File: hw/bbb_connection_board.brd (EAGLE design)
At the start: 20 x 64 mm, 11 parts, among them P8 MA23-2

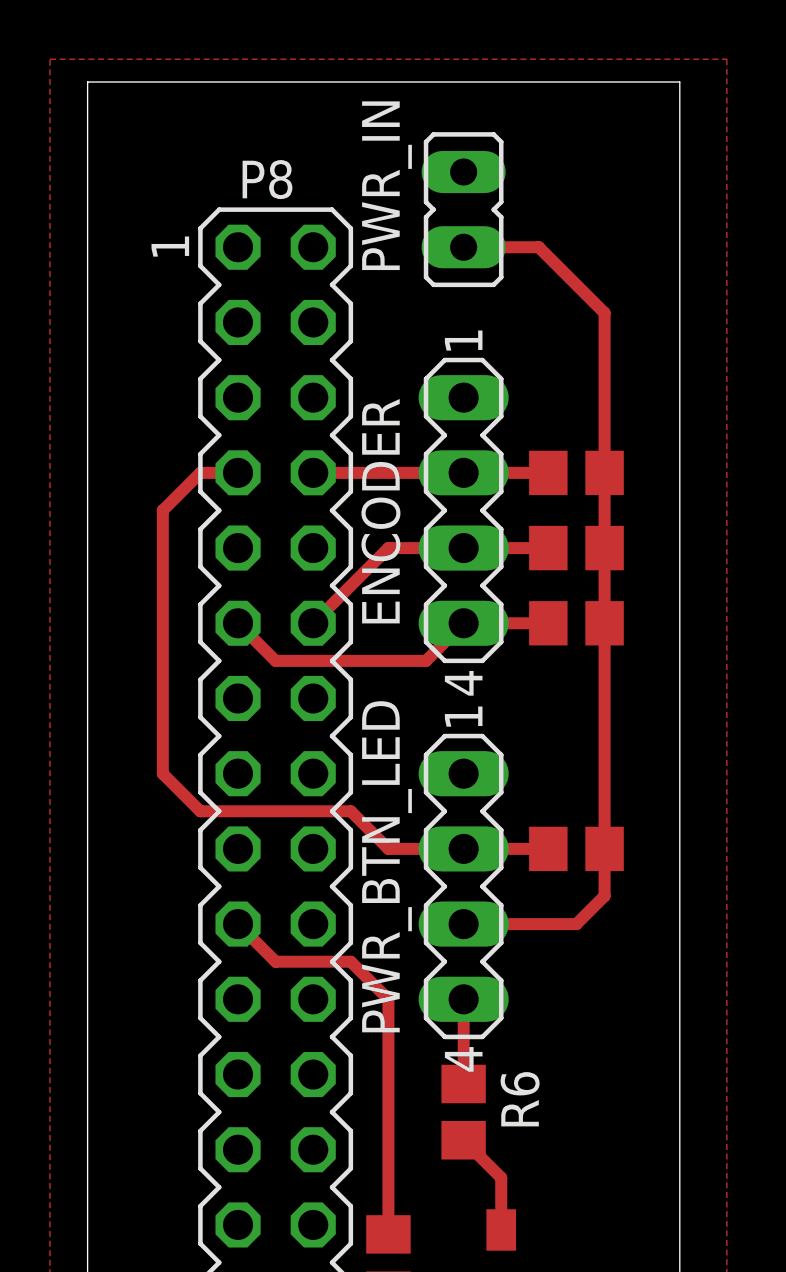
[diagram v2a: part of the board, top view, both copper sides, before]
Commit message: move connectors to bottom layer
the connector to the bbb also needs to be mounted on the bottom side, but can't be simply mirrored, since that would change the pinout
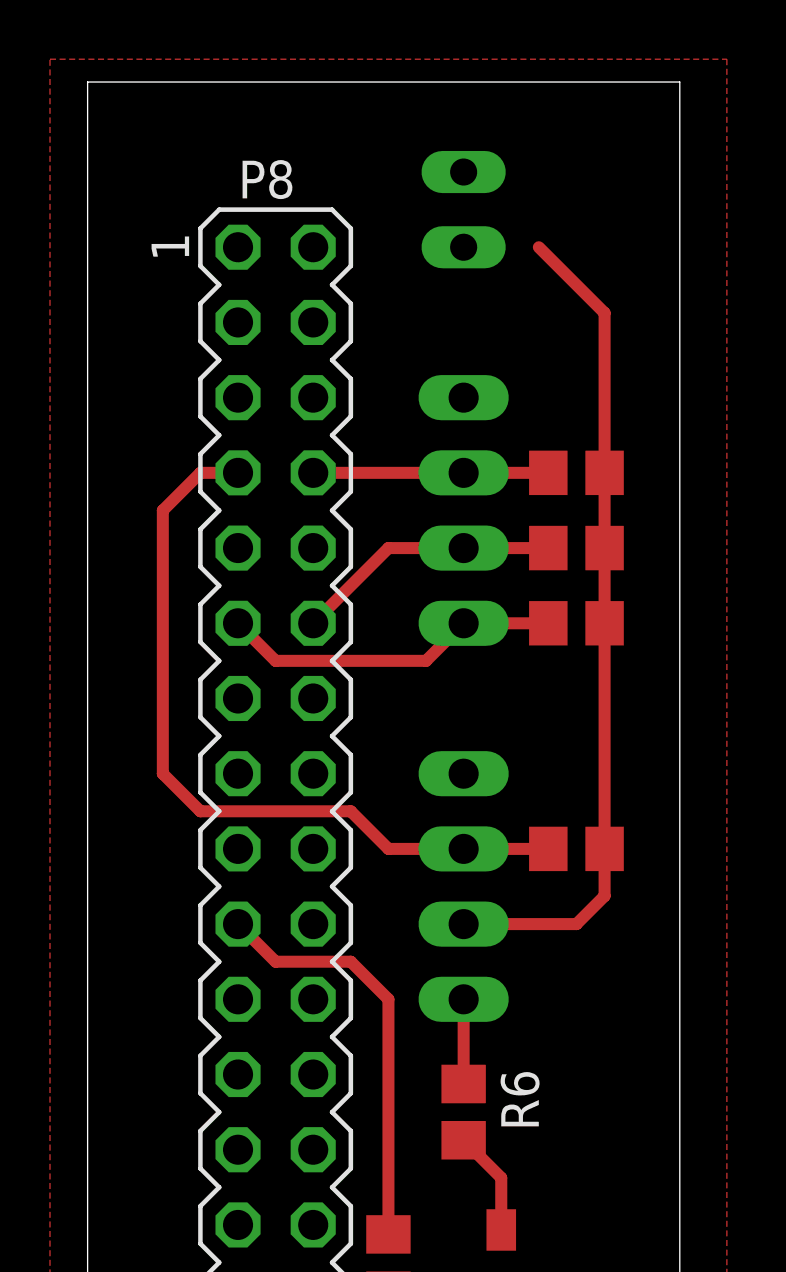
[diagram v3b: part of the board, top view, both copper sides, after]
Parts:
- flipped ENCODER to the bottom
- flipped PWR_BTN_LED to the bottom
- flipped PWR_IN to the bottom
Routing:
- net +3V3: track 30.5 -> 28.0 mm
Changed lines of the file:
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@@
 <attribute name="VALUE" x="2.159" y="5.08" size="1.27" layer="27" ratio="10" rot="R270"/>
 </element>
-<element name="PWR_IN" library="jumper" package="JP1" value="" x="12.7" y="59.69" smashed="yes" rot="R180">
-<attribute name="NAME" x="9.271" y="63.5" size="1.27" layer="25" ratio="10" rot="R270"/>
-<attribute name="VALUE" x="9.779" y="62.23" size="1.27" layer="27" ratio="10" rot="R270"/>
+<element name="PWR_IN" library="jumper" package="JP1" value="" x="12.7" y="59.69" smashed="yes" rot="MR180">
+<attribute name="NAME" x="14.351" y="55.88" size="1.27" layer="26" ratio="10" rot="MR90"/>
+<attribute name="VALUE" x="15.621" y="62.23" size="1.27" layer="28" ratio="10" rot="MR270"/>
 </element>
 <element name="R1" library="rcl" package="R0805" value="10k" x="16.51" y="38.1" smashed="yes">
@@
 <attribute name="VALUE" x="15.875" y="43.18" size="1.27" layer="27"/>
 </element>
-<element name="ENCODER" library="con-lstb" package="MA04-1" value="" x="12.7" y="49.53" smashed="yes" rot="R270">
-<attribute name="OC_NEWARK" value="unknown" x="12.7" y="49.53" size="1.778" layer="27" rot="R270" display="off"/>
-<attribute name="MPN" value="" x="12.7" y="49.53" size="1.778" layer="27" rot="R270" display="off"/>
-<attribute name="MF" value="" x="12.7" y="49.53" size="1.778" layer="27" rot="R270" display="off"/>
-<attribute name="OC_FARNELL" value="unknown" x="12.7" y="49.53" size="1.778" layer="27" rot="R270" display="off"/>
-<attribute name="NAME" x="9.271" y="53.34" size="1.27" layer="25" ratio="10" rot="R270"/>
-<attribute name="VALUE" x="14.351" y="48.895" size="1.27" layer="27" ratio="10" rot="R270"/>
+<element name="ENCODER" library="con-lstb" package="MA04-1" value="" x="12.7" y="49.53" smashed="yes" rot="MR270">
+<attribute name="OC_NEWARK" value="unknown" x="12.7" y="49.53" size="1.778" layer="28" rot="MR270" display="off"/>
+<attribute name="MPN" value="" x="12.7" y="49.53" size="1.778" layer="28" rot="MR270" display="off"/>
+<attribute name="MF" value="" x="12.7" y="49.53" size="1.778" layer="28" rot="MR270" display="off"/>
+<attribute name="OC_FARNELL" value="unknown" x="12.7" y="49.53" size="1.778" layer="28" rot="MR270" display="off"/>
+<attribute name="NAME" x="16.129" y="54.61" size="1.27" layer="26" ratio="10" rot="MR270"/>
+<attribute name="VALUE" x="11.049" y="48.895" size="1.27" layer="28" ratio="10" rot="MR270"/>
 </element>
-<element name="PWR_BTN_LED" library="con-lstb" package="MA04-1" value="" x="12.7" y="36.83" smashed="yes" rot="R270">
-<attribute name="OC_NEWARK" value="unknown" x="12.7" y="36.83" size="1.778" layer="27" rot="R270" display="off"/>
-<attribute name="MPN" value="" x="12.7" y="36.83" size="1.778" layer="27" rot="R270" display="off"/>
-<attribute name="MF" value="" x="12.7" y="36.83" size="1.778" layer="27" rot="R270" display="off"/>
-<attribute name="OC_FARNELL" value="unknown" x="12.7" y="36.83" size="1.778" layer="27" rot="R270" display="off"/>
-<attribute name="NAME" x="9.271" y="43.18" size="1.27" layer="25" ratio="10" rot="R270"/>
-<attribute name="VALUE" x="14.351" y="36.195" size="1.27" layer="27" ratio="10" rot="R270"/>
+<element name="PWR_BTN_LED" library="con-lstb" package="MA04-1" value="" x="12.7" y="36.83" smashed="yes" rot="MR270">
+<attribute name="OC_NEWARK" value="unknown" x="12.7" y="36.83" size="1.778" layer="28" rot="MR270" display="off"/>
+<attribute name="MPN" value="" x="12.7" y="36.83" size="1.778" layer="28" rot="MR270" display="off"/>
+<attribute name="MF" value="" x="12.7" y="36.83" size="1.778" layer="28" rot="MR270" display="off"/>
+<attribute name="OC_FARNELL" value="unknown" x="12.7" y="36.83" size="1.778" layer="28" rot="MR270" display="off"/>
+<attribute name="NAME" x="16.129" y="43.18" size="1.27" layer="26" ratio="10" rot="MR270"/>
+<attribute name="VALUE" x="11.049" y="36.195" size="1.27" layer="28" ratio="10" rot="MR270"/>
 </element>
 <element name="T1" library="transistor" package="SOT23-BEC" value="" x="13.97" y="24.13" smashed="yes">
@@
 <contactref element="R4" pad="2"/>
 <contactref element="PWR_BTN_LED" pad="3"/>
-<wire x1="12.7" y1="58.42" x2="15.24" y2="58.42" width="0.4064" layer="1"/>
 <wire x1="15.24" y1="58.42" x2="17.46" y2="56.2" width="0.4064" layer="1"/>
 <wire x1="17.46" y1="50.8" x2="17.46" y2="56.2" width="0.4064" layer="1"/>
@@
 <wire x1="17.46" y1="36.51" x2="16.51" y2="35.56" width="0.4064" layer="1"/>
 <wire x1="16.51" y1="35.56" x2="12.7" y2="35.56" width="0.4064" layer="1"/>
+<wire x1="15.24" y1="58.42" x2="12.7" y2="58.42" width="0" layer="19" extent="1-1"/>
 </signal>
 <signal name="PWR_LED">
@@
 <wire x1="5.08" y1="45.72" x2="6.35" y2="44.45" width="0.4064" layer="1"/>
 <wire x1="6.35" y1="44.45" x2="11.43" y2="44.45" width="0.4064" layer="1"/>
-<wire x1="11.43" y1="44.45" x2="12.7" y2="45.72" width="0.4064" layer="1"/>
 <wire x1="12.7" y1="45.72" x2="15.56" y2="45.72" width="0.4064" layer="1"/>
+<wire x1="12.7" y1="45.72" x2="11.43" y2="44.45" width="0.4064" layer="1"/>
 </signal>
 <signal name="ENCODER_A">
@@
 <contactref element="R3" pad="1"/>
 <contactref element="ENCODER" pad="3"/>
+<wire x1="7.62" y1="45.72" x2="10.16" y2="48.26" width="0.4064" layer="1"/>
+<wire x1="12.7" y1="48.26" x2="10.16" y2="48.26" width="0.4064" layer="1"/>
 <wire x1="12.7" y1="48.26" x2="15.56" y2="48.26" width="0.4064" layer="1"/>
-<wire x1="7.62" y1="45.72" x2="10.16" y2="48.26" width="0.4064" layer="1"/>
-<wire x1="10.16" y1="48.26" x2="12.7" y2="48.26" width="0.4064" layer="1"/>
 </signal>
 <signal name="PWR_BTN">

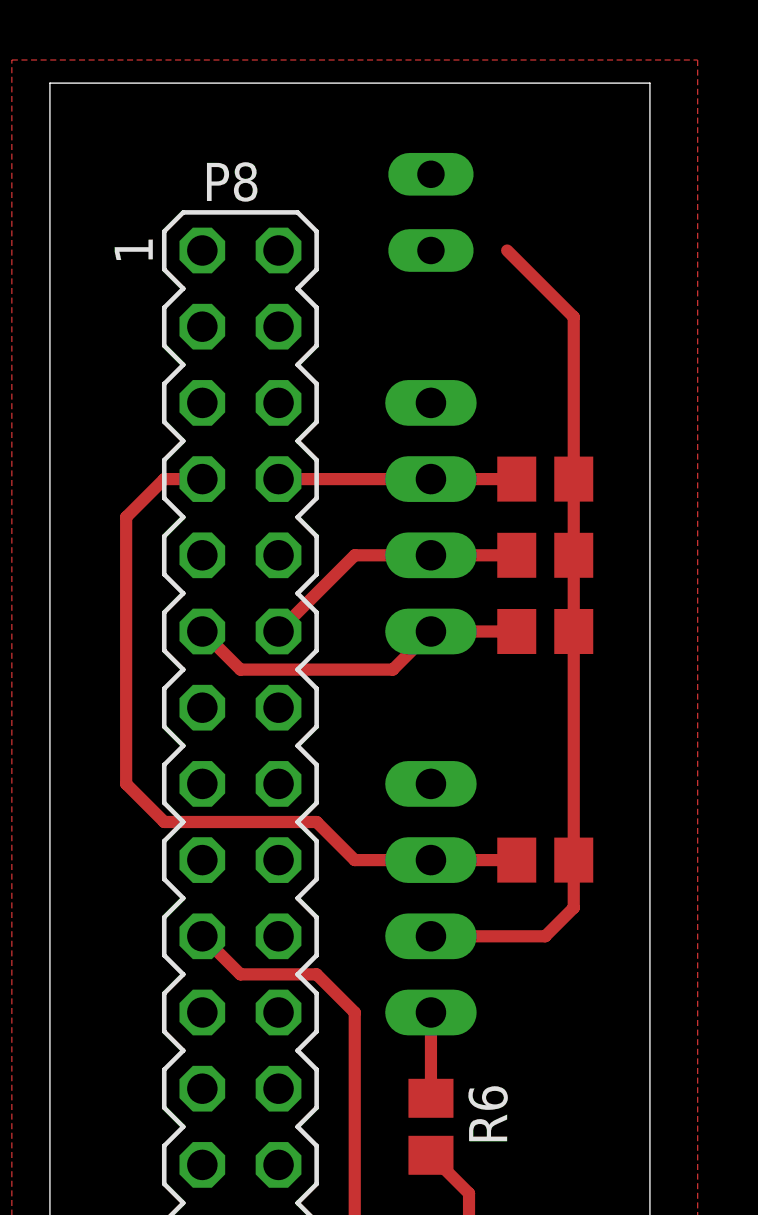
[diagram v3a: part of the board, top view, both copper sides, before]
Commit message: use angled pinheaders
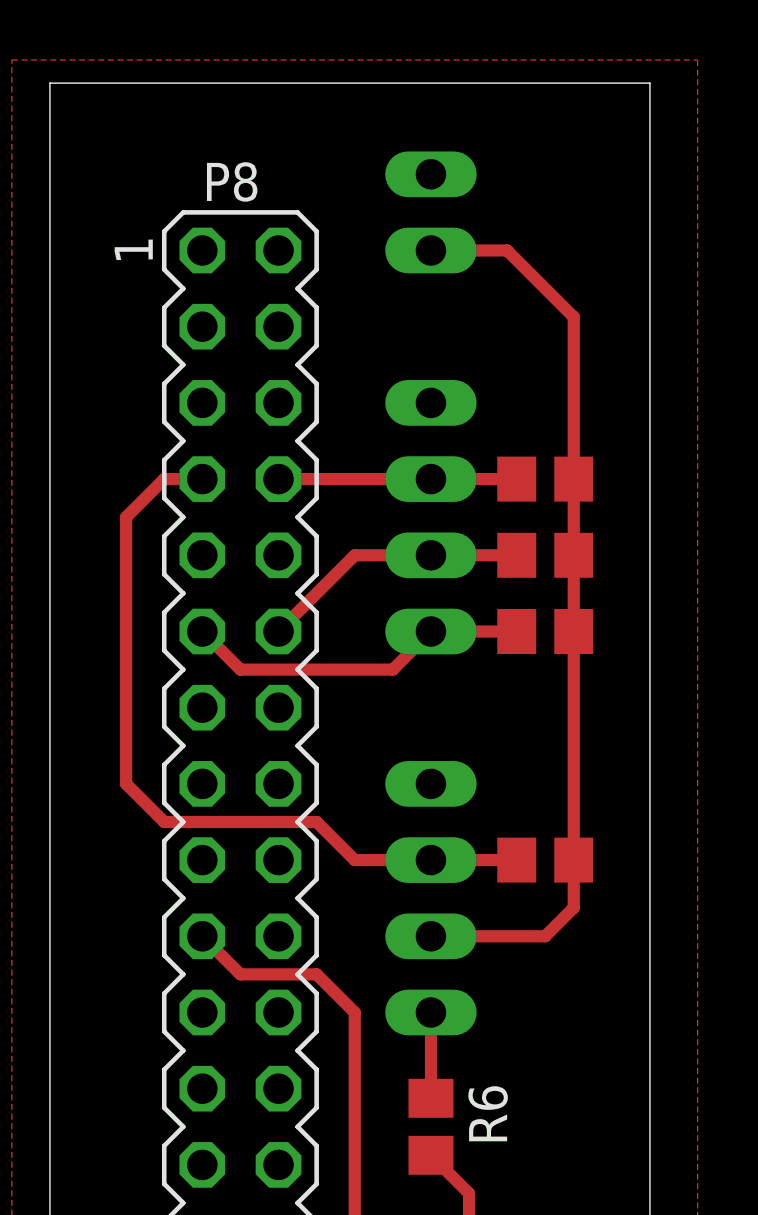
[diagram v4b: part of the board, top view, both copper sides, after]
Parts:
- removed PWR_BTN_LED: (no value), con-lstb:MA04-1
- removed PWR_IN: (no value), jumper:JP1
- added PWN_BTN_LED: (no value), pinhead:1X04/90
- added PWR_CON: (no value), pinhead:1X02/90
- ENCODER: device con-lstb:MA04-1 -> pinhead:1X04/90
- moved ENCODER 3.81 mm to (16.5, 49.5), turned to 90 degrees
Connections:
- net +3V3: now also PWN_BTN_LED.2, PWR_CON.1; no longer PWR_BTN_LED.3, PWR_IN.2
- net ENCODER_A: now also ENCODER.2; no longer ENCODER.3
- net ENCODER_B: now also ENCODER.1; no longer ENCODER.4
- net ENCODER_BTN: now also ENCODER.3; no longer ENCODER.2
- net GND: now also ENCODER.4, PWN_BTN_LED.4, PWR_CON.2; no longer ENCODER.1, PWR_BTN_LED.1, PWR_IN.1
- net LED_OUT: now also PWN_BTN_LED.1; no longer PWR_BTN_LED.4
- net PWR_BTN: now also PWN_BTN_LED.3; no longer PWR_BTN_LED.2
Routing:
- net +3V3: track 28.0 -> 30.5 mm
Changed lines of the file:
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@@
 <attribute name="VALUE" x="2.159" y="5.08" size="1.27" layer="27" ratio="10" rot="R270"/>
-</element>
-<element name="PWR_IN" library="jumper" package="JP1" value="" x="12.7" y="59.69" smashed="yes" rot="MR180">
-<attribute name="NAME" x="14.351" y="55.88" size="1.27" layer="26" ratio="10" rot="MR90"/>
-<attribute name="VALUE" x="15.621" y="62.23" size="1.27" layer="28" ratio="10" rot="MR270"/>
 </element>
 <element name="R1" library="rcl" package="R0805" value="10k" x="16.51" y="38.1" smashed="yes">
@@
 <attribute name="VALUE" x="15.875" y="43.18" size="1.27" layer="27"/>
 </element>
-<element name="ENCODER" library="con-lstb" package="MA04-1" value="" x="12.7" y="49.53" smashed="yes" rot="MR270">
-<attribute name="OC_NEWARK" value="unknown" x="12.7" y="49.53" size="1.778" layer="28" rot="MR270" display="off"/>
-<attribute name="MPN" value="" x="12.7" y="49.53" size="1.778" layer="28" rot="MR270" display="off"/>
-<attribute name="MF" value="" x="12.7" y="49.53" size="1.778" layer="28" rot="MR270" display="off"/>
-<attribute name="OC_FARNELL" value="unknown" x="12.7" y="49.53" size="1.778" layer="28" rot="MR270" display="off"/>
-<attribute name="NAME" x="16.129" y="54.61" size="1.27" layer="26" ratio="10" rot="MR270"/>
-<attribute name="VALUE" x="11.049" y="48.895" size="1.27" layer="28" ratio="10" rot="MR270"/>
-</element>
-<element name="PWR_BTN_LED" library="con-lstb" package="MA04-1" value="" x="12.7" y="36.83" smashed="yes" rot="MR270">
-<attribute name="OC_NEWARK" value="unknown" x="12.7" y="36.83" size="1.778" layer="28" rot="MR270" display="off"/>
-<attribute name="MPN" value="" x="12.7" y="36.83" size="1.778" layer="28" rot="MR270" display="off"/>
-<attribute name="MF" value="" x="12.7" y="36.83" size="1.778" layer="28" rot="MR270" display="off"/>
-<attribute name="OC_FARNELL" value="unknown" x="12.7" y="36.83" size="1.778" layer="28" rot="MR270" display="off"/>
-<attribute name="NAME" x="16.129" y="43.18" size="1.27" layer="26" ratio="10" rot="MR270"/>
-<attribute name="VALUE" x="11.049" y="36.195" size="1.27" layer="28" ratio="10" rot="MR270"/>
-</element>
 <element name="T1" library="transistor" package="SOT23-BEC" value="" x="13.97" y="24.13" smashed="yes">
 <attribute name="NAME" x="13.335" y="19.685" size="1.27" layer="25"/>
@@
 <attribute name="VALUE" x="15.24" y="28.575" size="1.27" layer="27" rot="R90"/>
 </element>
+<element name="PWR_CON" library="pinhead" package="1X02/90" value="" x="16.51" y="59.69" smashed="yes" rot="MR90">
+<attribute name="NAME" x="17.145" y="54.61" size="1.27" layer="26" ratio="10" rot="MR90"/>
+<attribute name="VALUE" x="12.7" y="64.135" size="1.27" layer="28" rot="MR180"/>
+</element>
+<element name="ENCODER" library="pinhead" package="1X04/90" value="" x="16.51" y="49.53" smashed="yes" rot="MR90">
+<attribute name="NAME" x="17.145" y="44.45" size="1.27" layer="26" ratio="10" rot="MR90"/>
+<attribute name="VALUE" x="12.065" y="56.515" size="1.27" layer="28" rot="MR180"/>
+</element>
+<element name="PWN_BTN_LED" library="pinhead" package="1X04/90" value="" x="16.51" y="36.83" smashed="yes" rot="MR90">
+<attribute name="NAME" x="17.145" y="30.48" size="1.27" layer="26" ratio="10" rot="MR90"/>
+<attribute name="VALUE" x="12.065" y="43.815" size="1.27" layer="28" rot="MR180"/>
+</element>
 </elements>
 <signals>
@@
 <contactref element="P8" pad="1"/>
 <contactref element="P8" pad="2"/>
-<contactref element="PWR_IN" pad="1"/>
 <polygon width="0.4064" layer="1">
 <vertex x="-1.27" y="64.77"/>
@@
 <vertex x="-1.27" y="-1.27"/>
 </polygon>
-<contactref element="ENCODER" pad="1"/>
-<contactref element="PWR_BTN_LED" pad="1"/>
 <contactref element="T1" pad="E"/>
+<contactref element="PWR_CON" pad="2"/>
+<contactref element="ENCODER" pad="4"/>
+<contactref element="PWN_BTN_LED" pad="4"/>
 </signal>
 <signal name="+3V3">
-<contactref element="PWR_IN" pad="2"/>
 <contactref element="R1" pad="2"/>
 <contactref element="R2" pad="2"/>
 <contactref element="R3" pad="2"/>
 <contactref element="R4" pad="2"/>
-<contactref element="PWR_BTN_LED" pad="3"/>
 <wire x1="15.24" y1="58.42" x2="17.46" y2="56.2" width="0.4064" layer="1"/>
 <wire x1="17.46" y1="50.8" x2="17.46" y2="56.2" width="0.4064" layer="1"/>
@@
 <wire x1="17.46" y1="38.1" x2="17.46" y2="36.51" width="0.4064" layer="1"/>
 <wire x1="17.46" y1="36.51" x2="16.51" y2="35.56" width="0.4064" layer="1"/>
-<wire x1="16.51" y1="35.56" x2="12.7" y2="35.56" width="0.4064" layer="1"/>
-<wire x1="15.24" y1="58.42" x2="12.7" y2="58.42" width="0" layer="19" extent="1-1"/>
+<contactref element="PWR_CON" pad="1"/>
+<wire x1="12.7" y1="58.42" x2="15.24" y2="58.42" width="0.4064" layer="1"/>
+<contactref element="PWN_BTN_LED" pad="2"/>
+<wire x1="12.7" y1="35.56" x2="16.51" y2="35.56" width="0.4064" layer="1"/>
 </signal>
 <signal name="PWR_LED">
@@
 <contactref element="P8" pad="11"/>
 <contactref element="R4" pad="1"/>
-<contactref element="ENCODER" pad="4"/>
 <wire x1="5.08" y1="45.72" x2="6.35" y2="44.45" width="0.4064" layer="1"/>
 <wire x1="6.35" y1="44.45" x2="11.43" y2="44.45" width="0.4064" layer="1"/>
+<contactref element="ENCODER" pad="1"/>
 <wire x1="12.7" y1="45.72" x2="15.56" y2="45.72" width="0.4064" layer="1"/>
-<wire x1="12.7" y1="45.72" x2="11.43" y2="44.45" width="0.4064" layer="1"/>
+<wire x1="11.43" y1="44.45" x2="12.7" y2="45.72" width="0.4064" layer="1"/>
 </signal>
 <signal name="ENCODER_A">
 <contactref element="P8" pad="12"/>
 <contactref element="R3" pad="1"/>
-<contactref element="ENCODER" pad="3"/>
 <wire x1="7.62" y1="45.72" x2="10.16" y2="48.26" width="0.4064" layer="1"/>
-<wire x1="12.7" y1="48.26" x2="10.16" y2="48.26" width="0.4064" layer="1"/>
+<contactref element="ENCODER" pad="2"/>
+<wire x1="10.16" y1="48.26" x2="12.7" y2="48.26" width="0.4064" layer="1"/>
 <wire x1="12.7" y1="48.26" x2="15.56" y2="48.26" width="0.4064" layer="1"/>
 </signal>
@@
 <contactref element="P8" pad="7"/>
 <contactref element="R1" pad="1"/>
-<contactref element="PWR_BTN_LED" pad="2"/>
 <wire x1="5.08" y1="50.8" x2="3.81" y2="50.8" width="0.4064" layer="1"/>
 <wire x1="3.81" y1="50.8" x2="2.54" y2="49.53" width="0.4064" layer="1"/>
@@
 <wire x1="3.81" y1="39.37" x2="8.89" y2="39.37" width="0.4064" layer="1"/>
 <wire x1="8.89" y1="39.37" x2="10.16" y2="38.1" width="0.4064" layer="1"/>
+<contactref element="PWN_BTN_LED" pad="3"/>
 <wire x1="10.16" y1="38.1" x2="12.7" y2="38.1" width="0.4064" layer="1"/>
 <wire x1="12.7" y1="38.1" x2="15.56" y2="38.1" width="0.4064" layer="1"/>
@@
 <contactref element="P8" pad="8"/>
 <contactref element="R2" pad="1"/>
-<contactref element="ENCODER" pad="2"/>
+<contactref element="ENCODER" pad="3"/>
 <wire x1="7.62" y1="50.8" x2="12.7" y2="50.8" width="0.4064" layer="1"/>
 <wire x1="12.7" y1="50.8" x2="15.56" y2="50.8" width="0.4064" layer="1"/>
@@
 <signal name="LED_OUT">
 <contactref element="R6" pad="2"/>
-<contactref element="PWR_BTN_LED" pad="4"/>
+<contactref element="PWN_BTN_LED" pad="1"/>
 <wire x1="12.7" y1="33.02" x2="12.7" y2="30.16" width="0.4064" layer="1"/>
 </signal>

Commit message: add missing values
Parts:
- T1: value (none) -> BC847C
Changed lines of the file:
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@@
 <attribute name="VALUE" x="15.875" y="43.18" size="1.27" layer="27"/>
 </element>
-<element name="T1" library="transistor" package="SOT23-BEC" value="" x="13.97" y="24.13" smashed="yes">
+<element name="T1" library="transistor" package="SOT23-BEC" value="BC847C" x="13.97" y="24.13" smashed="yes">
 <attribute name="NAME" x="13.335" y="19.685" size="1.27" layer="25"/>
 <attribute name="VALUE" x="12.065" y="20.955" size="1.27" layer="27"/>
